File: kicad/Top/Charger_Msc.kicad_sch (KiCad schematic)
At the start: 22 parts

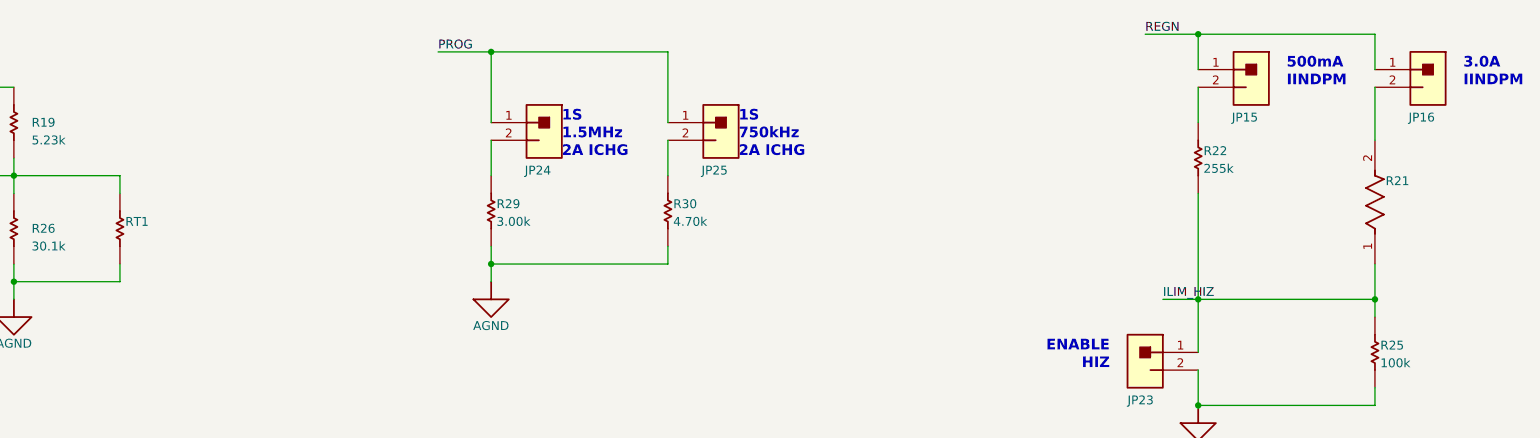
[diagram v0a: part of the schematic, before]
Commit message: Properly synced pcb to schematic
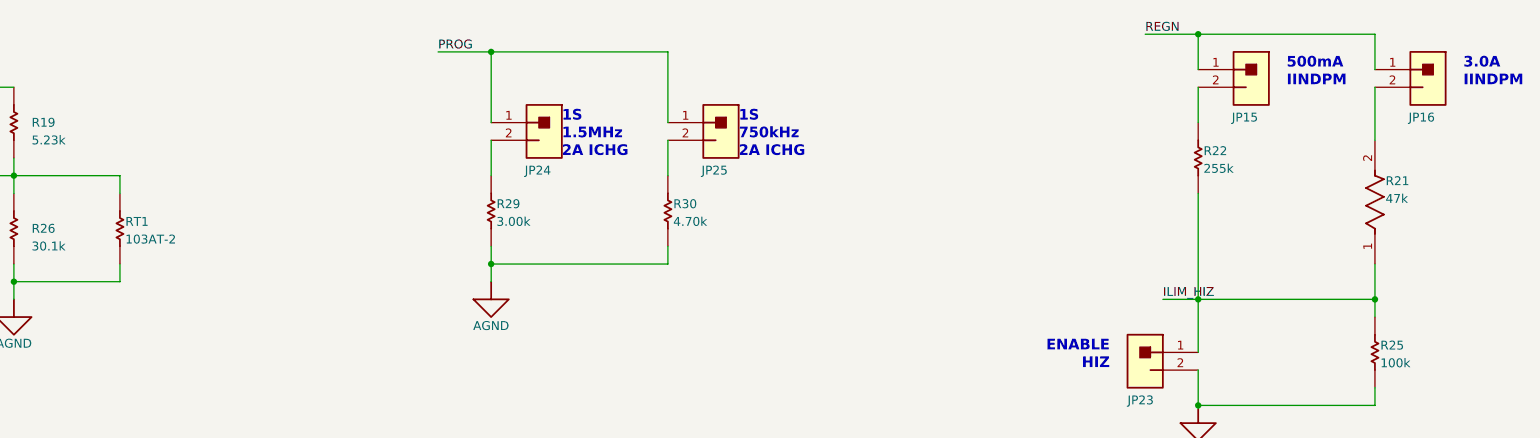
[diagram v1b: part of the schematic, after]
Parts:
- D13, D14: value ~ -> LTST-C190GKT; footprint LED_LTST-C190 -> AltiumImports:LED_LTST-C190
- JP14, JP15, JP16, JP23, JP24, JP25: value ~ -> CMP-0002337-1; footprint CONN_PEC02SAAN -> AltiumImports:CONN_PEC02SAAN
- JP19, JP34, JP35: value ~ -> Header_2x1; footprint CONN_PEC02SAAN -> AltiumImports:CONN_PEC02SAAN
- R19: value ~ -> CMP-0026464-2; footprint 0402 -> AltiumImports:0402
- R21: value ~ -> 47k; footprint FP-CRCW0603-e3-IPC_B -> AltiumImports:FP-CRCW0603-e3-IPC_B
- R22: value ~ -> CRCW0603255KFKEA; footprint 0603 -> AltiumImports:0603
- R25: value ~ -> RC0603FR-07100KL; footprint 0603 -> AltiumImports:0603
- R26: value ~ -> CMP-0026284-2; footprint 0402 -> AltiumImports:0402
- R29: value ~ -> RC0603FR-073KL; footprint 0603 -> AltiumImports:0603
- R30: value ~ -> RC0603FR-074K7L; footprint 0603 -> AltiumImports:0603
- R40, R41: value ~ -> CRCW04022K21FKED; footprint 0402 -> AltiumImports:0402
- RT1: value ~ -> 103AT-2; footprint SEMI-103AT-2_V -> AltiumImports:SEMI-103AT-2_V
- S1: value ~ -> CMP-0002170-2; footprint KSR -> AltiumImports:KSR
